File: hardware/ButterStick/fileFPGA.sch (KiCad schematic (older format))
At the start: 3 parts, among them U3 ECP5U25, X1 ASDMB

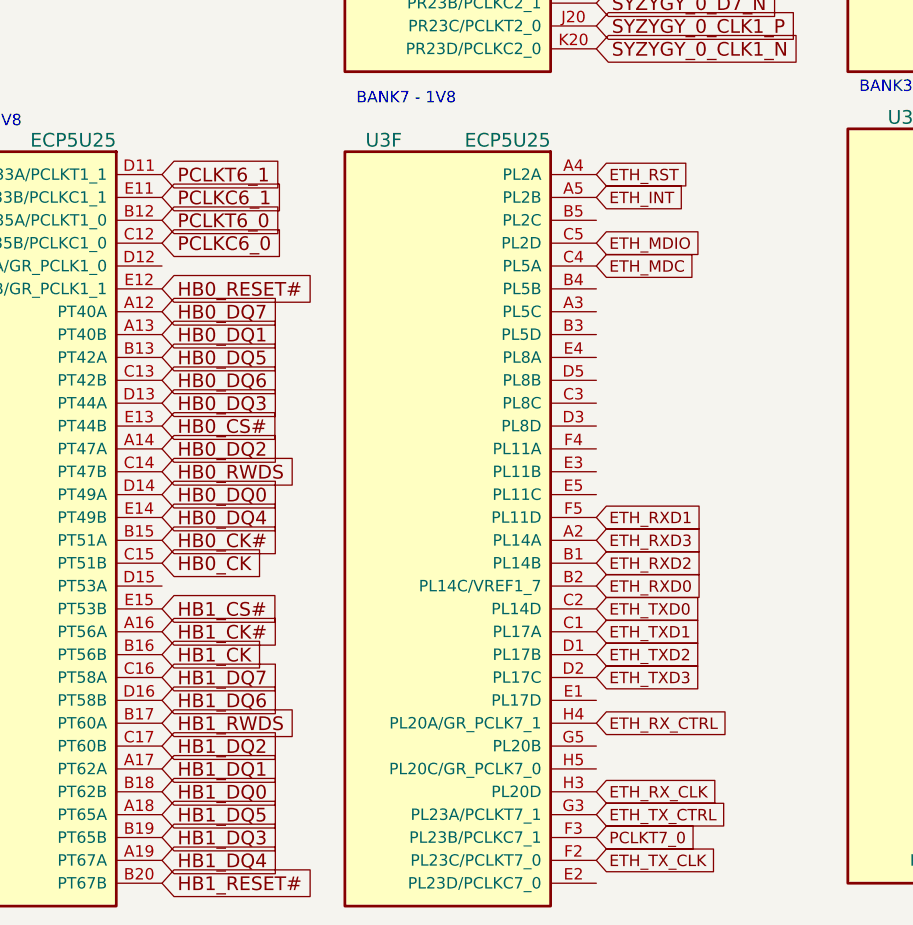
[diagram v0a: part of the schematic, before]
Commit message: Update Board.  - Added more signal breakouts  - Tidy up some pairs  - Neaten up some length matching.  - Connect RGMII
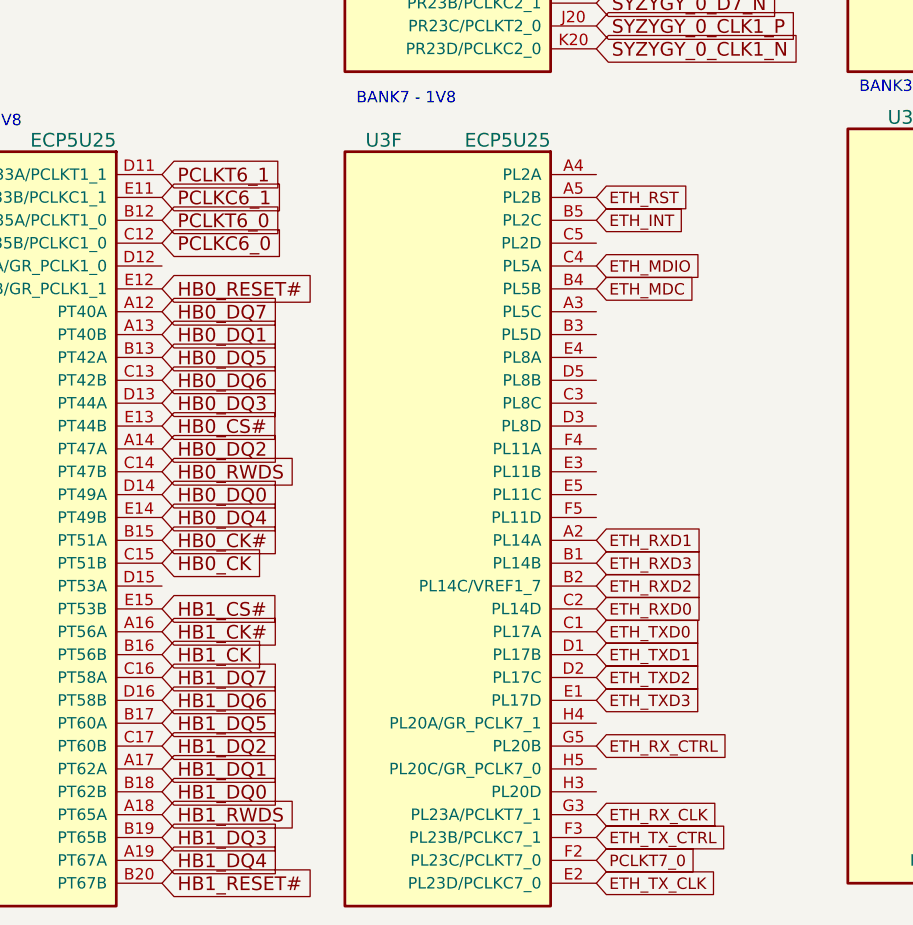
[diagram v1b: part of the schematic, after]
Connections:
- net ETH_INT: now also U3.B5 (PL2C); no longer U3.A5 (PL2B)
- net ETH_MDC: now also U3.B4 (PL5B); no longer U3.C4 (PL5A)
- net ETH_MDIO: now also U3.C4 (PL5A); no longer U3.C5 (PL2D)
- net ETH_RST: now also U3.A5 (PL2B); no longer U3.A4 (PL2A)
- net ETH_RXD0: now also U3.C2 (PL14D); no longer U3.B2 (PL14C/VREF1_7)
- net ETH_RXD1: now also U3.A2 (PL14A); no longer U3.F5 (PL11D)
- net ETH_RXD2: now also U3.B2 (PL14C/VREF1_7); no longer U3.B1 (PL14B)
- net ETH_RXD3: now also U3.B1 (PL14B); no longer U3.A2 (PL14A)
- net ETH_RX_CLK: now also U3.G3 (PL23A/PCLKT7_1); no longer U3.H3 (PL20D)
- net ETH_RX_CTRL: now also U3.G5 (PL20B); no longer U3.H4 (PL20A/GR_PCLK7_1)
- net ETH_TXD0: now also U3.C1 (PL17A); no longer U3.C2 (PL14D)
- net ETH_TXD1: now also U3.D1 (PL17B); no longer U3.C1 (PL17A)
- net ETH_TXD2: now also U3.D2 (PL17C); no longer U3.D1 (PL17B)
- net ETH_TXD3: now also U3.E1 (PL17D); no longer U3.D2 (PL17C)
- net ETH_TX_CLK: now also U3.E2 (PL23D/PCLKC7_0); no longer U3.F2 (PL23C/PCLKT7_0)
- net ETH_TX_CTRL: now also U3.F3 (PL23B/PCLKC7_1); no longer U3.G3 (PL23A/PCLKT7_1)
- net HB1_DQ5: now also U3.B17 (PT60A); no longer U3.A18 (PT65A)
- net HB1_RWDS: now also U3.A18 (PT65A); no longer U3.B17 (PT60A)
- net PCLKT7_0: now also U3.F2 (PL23C/PCLKT7_0); no longer U3.F3 (PL23B/PCLKC7_1)
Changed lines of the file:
@@
 Text GLabel 1950 7500 2    60   Input ~ 0
 HB1_DQ4
-Text GLabel 1950 7300 2    60   Input ~ 0
+Text GLabel 1950 6900 2    60   Input ~ 0
 HB1_DQ5
 Text GLabel 1950 6800 2    60   Input ~ 0
@@
 Text GLabel 1950 6700 2    60   Input ~ 0
 HB1_DQ7
-Text GLabel 1950 6900 2    60   Input ~ 0
+Text GLabel 1950 7300 2    60   Input ~ 0
 HB1_RWDS
 Wire Wire Line
@@
 Wire Wire Line
 	10000 1600 10000 1650
+Text GLabel 3850 5000 2    50   Input ~ 0
+ETH_MDC
 Text GLabel 3850 4900 2    50   Input ~ 0
-ETH_MDC
-Text GLabel 3850 4800 2    50   Input ~ 0
 ETH_MDIO
+Text GLabel 3850 6500 2    50   Input ~ 0
+ETH_TXD0
+Text GLabel 3850 6600 2    50   Input ~ 0
+ETH_TXD1
+Text GLabel 3850 6700 2    50   Input ~ 0
+ETH_TXD2
+Text GLabel 3850 6800 2    50   Input ~ 0
+ETH_TXD3
 Text GLabel 3850 6400 2    50   Input ~ 0
-ETH_TXD0
-Text GLabel 3850 6500 2    50   Input ~ 0
-ETH_TXD1
-Text GLabel 3850 6600 2    50   Input ~ 0
-ETH_TXD2
-Text GLabel 3850 6700 2    50   Input ~ 0
-ETH_TXD3
+ETH_RXD0
+Text GLabel 3850 6100 2    50   Input ~ 0
+ETH_RXD1
 Text GLabel 3850 6300 2    50   Input ~ 0
-ETH_RXD0
-Text GLabel 3850 6000 2    50   Input ~ 0
-ETH_RXD1
+ETH_RXD2
 Text GLabel 3850 6200 2    50   Input ~ 0
-ETH_RXD2
-Text GLabel 3850 6100 2    50   Input ~ 0
 ETH_RXD3
+Text GLabel 3850 7400 2    50   Input ~ 0
+ETH_TX_CTRL
+Text GLabel 3850 7600 2    50   Input ~ 0
+ETH_TX_CLK
+Text GLabel 3850 7000 2    50   Input ~ 0
+ETH_RX_CTRL
 Text GLabel 3850 7300 2    50   Input ~ 0
-ETH_TX_CTRL
-Text GLabel 3850 7500 2    50   Input ~ 0
-ETH_TX_CLK
-Text GLabel 3850 6900 2    50   Input ~ 0
-ETH_RX_CTRL
-Text GLabel 3850 7200 2    50   Input ~ 0
 ETH_RX_CLK
-Text GLabel 3850 4600 2    50   Input ~ 0
+Text GLabel 3850 4700 2    50   Input ~ 0
 ETH_INT
 Text GLabel 9600 6200 2    60   Input ~ 0
@@
 Text GLabel -700 3750 2    50   Input ~ 0
 DISP0_DISP
-Text GLabel 3850 4500 2    50   Input ~ 0
+Text GLabel 3850 4600 2    50   Input ~ 0
 ETH_RST
 Text GLabel 1950 4800 2    60   Input ~ 0
@@
 Text GLabel 1950 4500 2    60   Input ~ 0
 PCLKT6_1
-Text GLabel 3850 7400 2    50   Input ~ 0
+Text GLabel 3850 7500 2    50   Input ~ 0
 PCLKT7_0
 Text GLabel 3850 2050 2    60   Input ~ 0
@@
 	9650 4800 9650 4550
 $Comp
-L gkl_power:+3V3 #PWR?
+L gkl_power:+3V3 #PWR0106
 U 1 1 5C7C78F9
 P 9650 4550
-F 0 "#PWR?" H 9650 4400 50  0001 C CNN
+F 0 "#PWR0106" H 9650 4400 50  0001 C CNN
 F 1 "+3V3" V 9650 4750 50  0000 C CNN
 F 2 "" H 9650 4550 50  0001 C CNN
@@
 	8800 5700 8600 5700
 $Comp
-L gkl_power:GND #PWR?
+L gkl_power:GND #PWR0123
 U 1 1 5C7CB5AD
 P 7750 5900
-F 0 "#PWR?" H 7750 5650 50  0001 C CNN
+F 0 "#PWR0123" H 7750 5650 50  0001 C CNN
 F 1 "GND" H 7753 5774 50  0000 C CNN
 F 2 "" H 7650 5550 50  0001 C CNN

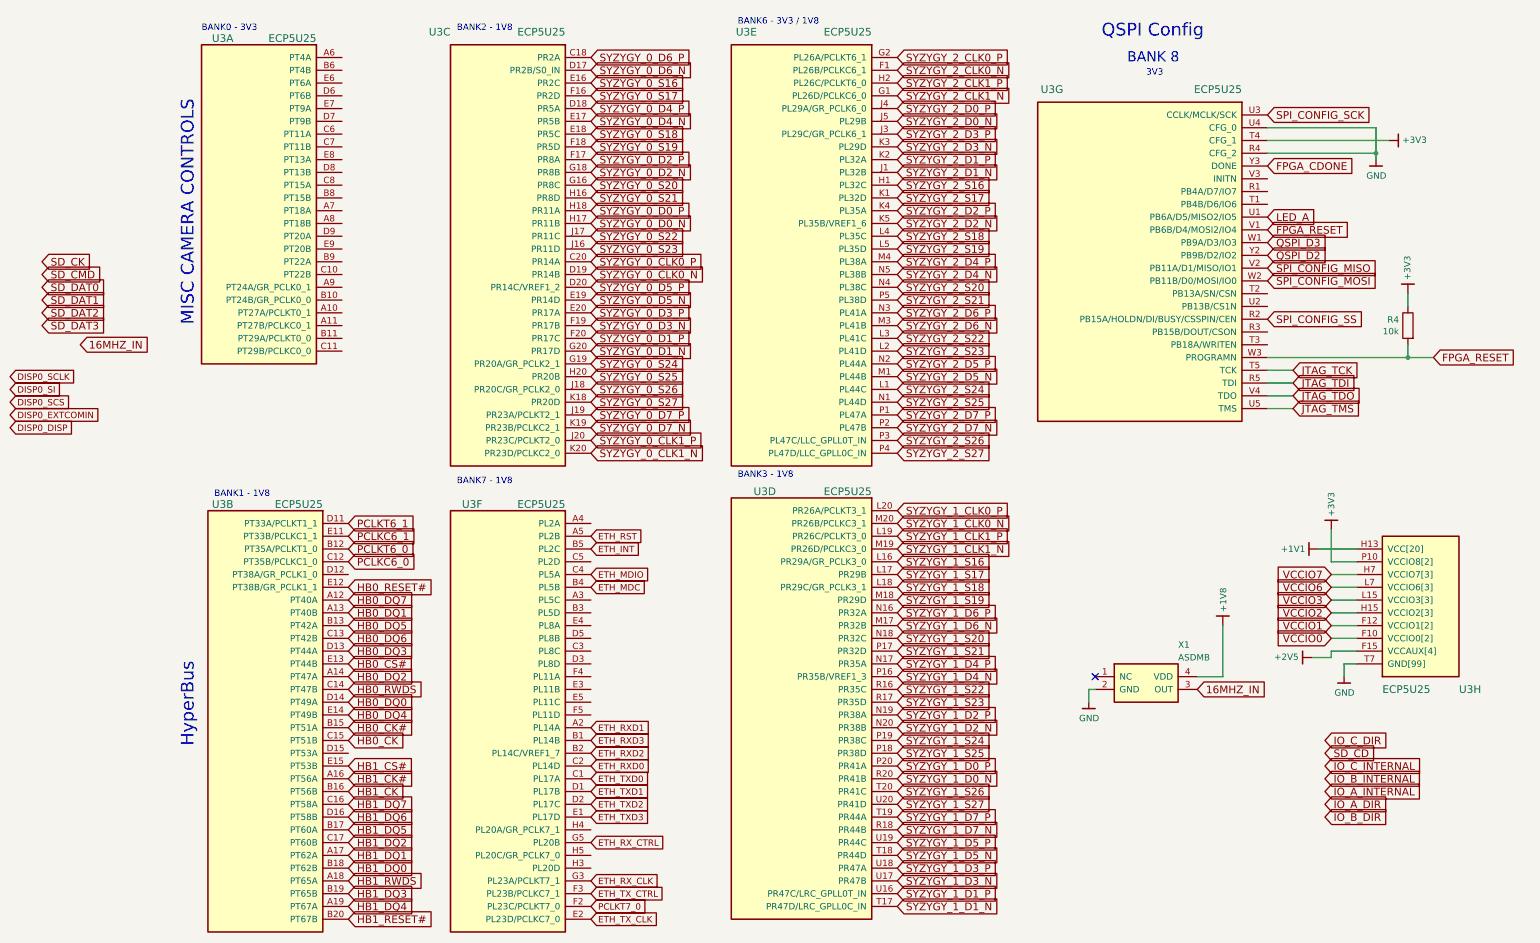
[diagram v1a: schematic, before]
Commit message: Updated PCB. Routed all SYZYGY signals needed from the FPGA.
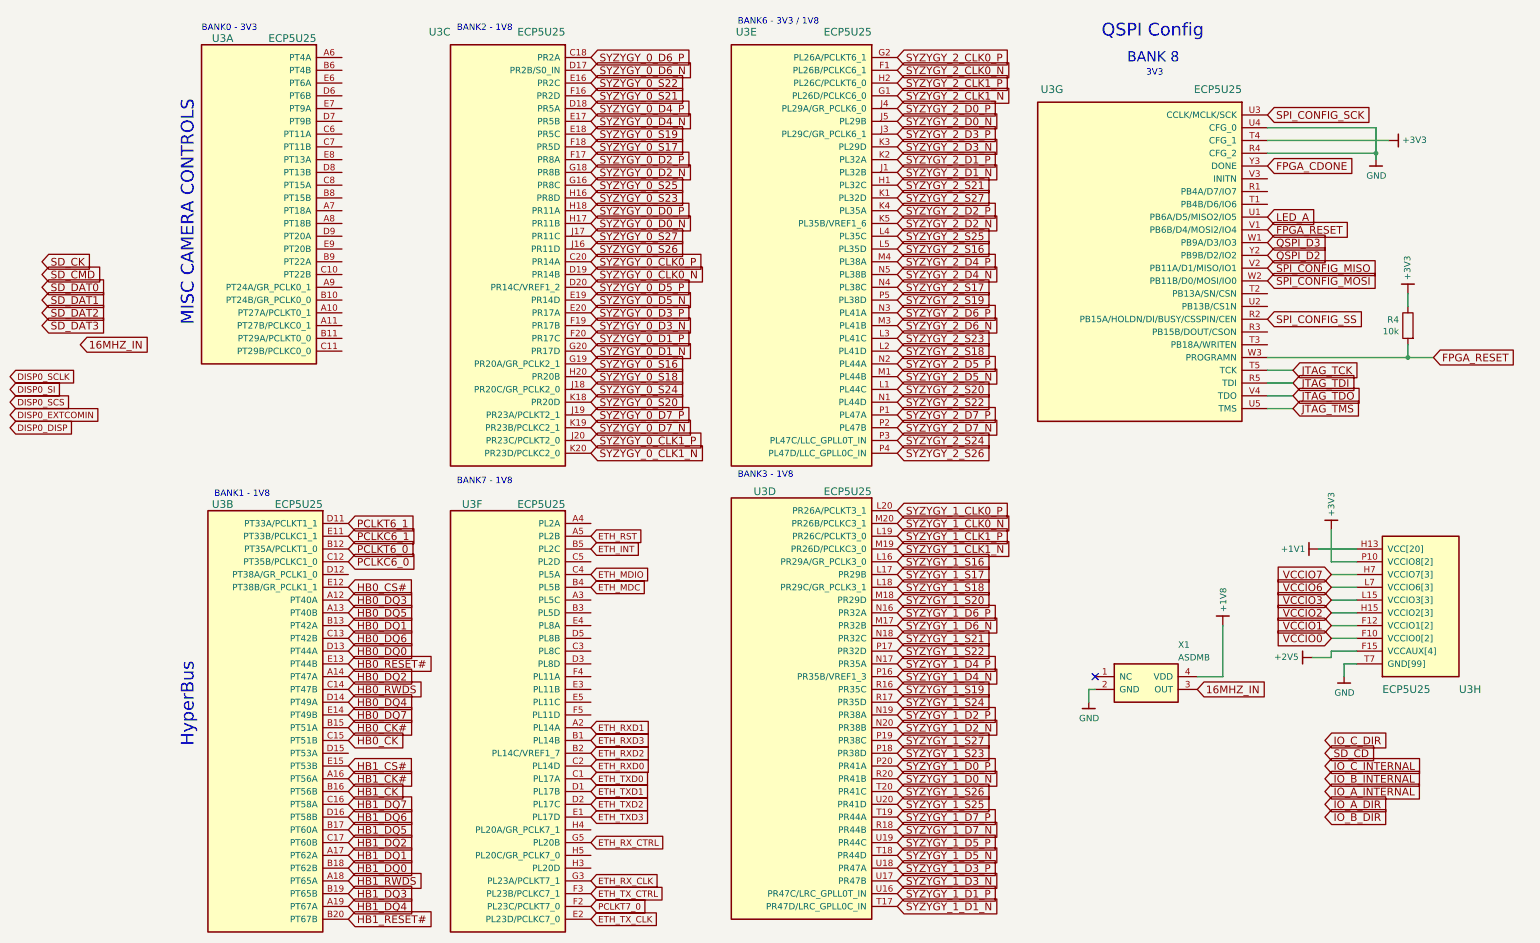
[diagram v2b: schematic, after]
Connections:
- net HB0_CS#: now also U3.E12 (PT38B/GR_PCLK1_1); no longer U3.E13 (PT44B)
- net HB0_DQ0: now also U3.D13 (PT44A); no longer U3.D14 (PT49A)
- net HB0_DQ1: now also U3.B13 (PT42A); no longer U3.A13 (PT40B)
- net HB0_DQ3: now also U3.A12 (PT40A); no longer U3.D13 (PT44A)
- net HB0_DQ4: now also U3.D14 (PT49A); no longer U3.E14 (PT49B)
- net HB0_DQ5: now also U3.A13 (PT40B); no longer U3.B13 (PT42A)
- net HB0_DQ7: now also U3.E14 (PT49B); no longer U3.A12 (PT40A)
- net HB0_RESET#: now also U3.E13 (PT44B); no longer U3.E12 (PT38B/GR_PCLK1_1)
- net SYZYGY_0_S16: now also U3.G19 (PR20A/GR_PCLK2_1); no longer U3.E16 (PR2C)
- net SYZYGY_0_S17: now also U3.F18 (PR5D); no longer U3.F16 (PR2D)
- net SYZYGY_0_S18: now also U3.H20 (PR20B); no longer U3.E18 (PR5C)
- net SYZYGY_0_S19: now also U3.E18 (PR5C); no longer U3.F18 (PR5D)
- net SYZYGY_0_S20: now also U3.K18 (PR20D); no longer U3.G16 (PR8C)
- net SYZYGY_0_S21: now also U3.F16 (PR2D); no longer U3.H16 (PR8D)
- net SYZYGY_0_S22: now also U3.E16 (PR2C); no longer U3.J17 (PR11C)
- net SYZYGY_0_S23: now also U3.H16 (PR8D); no longer U3.J16 (PR11D)
- net SYZYGY_0_S24: now also U3.J18 (PR20C/GR_PCLK2_0); no longer U3.G19 (PR20A/GR_PCLK2_1)
- net SYZYGY_0_S25: now also U3.G16 (PR8C); no longer U3.H20 (PR20B)
- net SYZYGY_0_S26: now also U3.J16 (PR11D); no longer U3.J18 (PR20C/GR_PCLK2_0)
- net SYZYGY_0_S27: now also U3.J17 (PR11C); no longer U3.K18 (PR20D)
- net SYZYGY_1_S19: now also U3.R16 (PR35C); no longer U3.M18 (PR29D)
- net SYZYGY_1_S20: now also U3.M18 (PR29D); no longer U3.N18 (PR32C)
- net SYZYGY_1_S21: now also U3.N18 (PR32C); no longer U3.P17 (PR32D)
- net SYZYGY_1_S22: now also U3.P17 (PR32D); no longer U3.R16 (PR35C)
- net SYZYGY_1_S23: now also U3.P18 (PR38D); no longer U3.R17 (PR35D)
- net SYZYGY_1_S24: now also U3.R17 (PR35D); no longer U3.P19 (PR38C)
- net SYZYGY_1_S25: now also U3.U20 (PR41D); no longer U3.P18 (PR38D)
- net SYZYGY_1_S27: now also U3.P19 (PR38C); no longer U3.U20 (PR41D)
- net SYZYGY_2_S16: now also U3.L5 (PL35D); no longer U3.H1 (PL32C)
- net SYZYGY_2_S17: now also U3.N4 (PL38C); no longer U3.K1 (PL32D)
- net SYZYGY_2_S18: now also U3.L2 (PL41D); no longer U3.L4 (PL35C)
- net SYZYGY_2_S19: now also U3.P5 (PL38D); no longer U3.L5 (PL35D)
- net SYZYGY_2_S20: now also U3.L1 (PL44C); no longer U3.N4 (PL38C)
- net SYZYGY_2_S21: now also U3.H1 (PL32C); no longer U3.P5 (PL38D)
- net SYZYGY_2_S22: now also U3.N1 (PL44D); no longer U3.L3 (PL41C)
- net SYZYGY_2_S23: now also U3.L3 (PL41C); no longer U3.L2 (PL41D)
- net SYZYGY_2_S24: now also U3.P3 (PL47C/LLC_GPLL0T_IN); no longer U3.L1 (PL44C)
- net SYZYGY_2_S25: now also U3.L4 (PL35C); no longer U3.N1 (PL44D)
- net SYZYGY_2_S26: now also U3.P4 (PL47D/LLC_GPLL0C_IN); no longer U3.P3 (PL47C/LLC_GPLL0T_IN)
- net SYZYGY_2_S27: now also U3.K1 (PL32D); no longer U3.P4 (PL47D/LLC_GPLL0C_IN)
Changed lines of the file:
@@
 Text GLabel 9600 6300 2    60   Input ~ 0
 SD_CD
+Text GLabel 1950 5000 2    60   Input ~ 0
+HB0_CS#
 Text GLabel 1950 5600 2    60   Input ~ 0
-HB0_CS#
-Text GLabel 1950 5000 2    60   Input ~ 0
 HB0_RESET#
 Text GLabel 1950 6200 2    60   Input ~ 0
@@
 Text GLabel 1950 6100 2    60   Input ~ 0
 HB0_CK#
-Text GLabel 1950 5900 2    60   Input ~ 0
+Text GLabel 1950 5500 2    60   Input ~ 0
 HB0_DQ0
-Text GLabel 1950 5200 2    60   Input ~ 0
+Text GLabel 1950 5300 2    60   Input ~ 0
 HB0_DQ1
 Text GLabel 1950 5700 2    60   Input ~ 0
 HB0_DQ2
-Text GLabel 1950 5500 2    60   Input ~ 0
+Text GLabel 1950 5100 2    60   Input ~ 0
 HB0_DQ3
-Text GLabel 1950 6000 2    60   Input ~ 0
+Text GLabel 1950 5900 2    60   Input ~ 0
 HB0_DQ4
-Text GLabel 1950 5300 2    60   Input ~ 0
+Text GLabel 1950 5200 2    60   Input ~ 0
 HB0_DQ5
 Text GLabel 1950 5400 2    60   Input ~ 0
 HB0_DQ6
-Text GLabel 1950 5100 2    60   Input ~ 0
+Text GLabel 1950 6000 2    60   Input ~ 0
 HB0_DQ7
 Text GLabel 9150 2900 2    60   Input ~ 0
@@
 Text GLabel 3850 3650 2    60   Input ~ 0
 SYZYGY_0_D7_P
+Text GLabel 3850 3250 2    60   Input ~ 0
+SYZYGY_0_S16
+Text GLabel 3850 1550 2    60   Input ~ 0
+SYZYGY_0_S17
+Text GLabel 3850 3350 2    60   Input ~ 0
+SYZYGY_0_S18
+Text GLabel 3850 1450 2    60   Input ~ 0
+SYZYGY_0_S19
+Text GLabel 3850 3550 2    60   Input ~ 0
+SYZYGY_0_S20
+Text GLabel 3850 1150 2    60   Input ~ 0
+SYZYGY_0_S21
 Text GLabel 3850 1050 2    60   Input ~ 0
-SYZYGY_0_S16
-Text GLabel 3850 1150 2    60   Input ~ 0
-SYZYGY_0_S17
-Text GLabel 3850 1450 2    60   Input ~ 0
-SYZYGY_0_S18
-Text GLabel 3850 1550 2    60   Input ~ 0
-SYZYGY_0_S19
+SYZYGY_0_S22
+Text GLabel 3850 1950 2    60   Input ~ 0
+SYZYGY_0_S23
+Text GLabel 3850 3450 2    60   Input ~ 0
+SYZYGY_0_S24
 Text GLabel 3850 1850 2    60   Input ~ 0
-SYZYGY_0_S20
-Text GLabel 3850 1950 2    60   Input ~ 0
-SYZYGY_0_S21
+SYZYGY_0_S25
+Text GLabel 3850 2350 2    60   Input ~ 0
+SYZYGY_0_S26
 Text GLabel 3850 2250 2    60   Input ~ 0
-SYZYGY_0_S22
-Text GLabel 3850 2350 2    60   Input ~ 0
-SYZYGY_0_S23
-Text GLabel 3850 3250 2    60   Input ~ 0
-SYZYGY_0_S24
-Text GLabel 3850 3350 2    60   Input ~ 0
-SYZYGY_0_S25
-Text GLabel 3850 3450 2    60   Input ~ 0
-SYZYGY_0_S26
-Text GLabel 3850 3550 2    60   Input ~ 0
 SYZYGY_0_S27
 Text GLabel 6250 6400 2    60   Input ~ 0
@@
 Text GLabel 6250 3650 2    60   Input ~ 0
 SYZYGY_2_D7_P
+Text GLabel 6250 2350 2    60   Input ~ 0
+SYZYGY_2_S16
+Text GLabel 6250 2650 2    60   Input ~ 0
+SYZYGY_2_S17
+Text GLabel 6250 3150 2    60   Input ~ 0
+SYZYGY_2_S18
+Text GLabel 6250 2750 2    60   Input ~ 0
+SYZYGY_2_S19
+Text GLabel 6250 3450 2    60   Input ~ 0
+SYZYGY_2_S20
 Text GLabel 6250 1850 2    60   Input ~ 0
-SYZYGY_2_S16
+SYZYGY_2_S21
+Text GLabel 6250 3550 2    60   Input ~ 0
+SYZYGY_2_S22
+Text GLabel 6250 3050 2    60   Input ~ 0
+SYZYGY_2_S23
+Text GLabel 6250 3850 2    60   Input ~ 0
+SYZYGY_2_S24
+Text GLabel 6250 2250 2    60   Input ~ 0
+SYZYGY_2_S25
+Text GLabel 6250 3950 2    60   Input ~ 0
+SYZYGY_2_S26
 Text GLabel 6250 1950 2    60   Input ~ 0
-SYZYGY_2_S17
-Text GLabel 6250 2250 2    60   Input ~ 0
-SYZYGY_2_S18
-Text GLabel 6250 2350 2    60   Input ~ 0
-SYZYGY_2_S19
-Text GLabel 6250 2650 2    60   Input ~ 0
-SYZYGY_2_S20
-Text GLabel 6250 2750 2    60   Input ~ 0
-SYZYGY_2_S21
-Text GLabel 6250 3050 2    60   Input ~ 0
-SYZYGY_2_S22
-Text GLabel 6250 3150 2    60   Input ~ 0
-SYZYGY_2_S23
-Text GLabel 6250 3450 2    60   Input ~ 0
-SYZYGY_2_S24
-Text GLabel 6250 3550 2    60   Input ~ 0
-SYZYGY_2_S25
-Text GLabel 6250 3850 2    60   Input ~ 0
-SYZYGY_2_S26
-Text GLabel 6250 3950 2    60   Input ~ 0
 SYZYGY_2_S27
 Text GLabel 6250 4800 2    60   Input ~ 0
@@
 Text GLabel 6250 5000 2    60   Input ~ 0
 SYZYGY_1_S18
+Text GLabel 6250 5800 2    60   Input ~ 0
+SYZYGY_1_S19
 Text GLabel 6250 5100 2    60   Input ~ 0
-SYZYGY_1_S19
+SYZYGY_1_S20
 Text GLabel 6250 5400 2    60   Input ~ 0
-SYZYGY_1_S20
+SYZYGY_1_S21
 Text GLabel 6250 5500 2    60   Input ~ 0
-SYZYGY_1_S21
-Text GLabel 6250 5800 2    60   Input ~ 0
 SYZYGY_1_S22
+Text GLabel 6250 6300 2    60   Input ~ 0
+SYZYGY_1_S23
 Text GLabel 6250 5900 2    60   Input ~ 0
-SYZYGY_1_S23
-Text GLabel 6250 6200 2    60   Input ~ 0
 SYZYGY_1_S24
-Text GLabel 6250 6300 2    60   Input ~ 0
+Text GLabel 6250 6700 2    60   Input ~ 0
 SYZYGY_1_S25
 Text GLabel 6250 6600 2    60   Input ~ 0
 SYZYGY_1_S26
-Text GLabel 6250 6700 2    60   Input ~ 0
+Text GLabel 6250 6200 2    60   Input ~ 0
 SYZYGY_1_S27
 $Comp
